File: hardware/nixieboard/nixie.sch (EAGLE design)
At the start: 60 parts

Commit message: added connectors to nixieboard for stability
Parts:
- added SV3, SV4: (no value), con-lstb:MA03-2
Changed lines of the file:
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@@
 <?xml version="1.0" encoding="utf-8"?>
 <!DOCTYPE eagle SYSTEM "eagle.dtd">
-<eagle version="7.2.0">
+<eagle version="6.5.0">
 <drawing>
 <settings>
@@
 <part name="SJ5" library="jumper" deviceset="SJ" device=""/>
 <part name="SJ6" library="jumper" deviceset="SJ" device=""/>
+<part name="SV3" library="con-lstb" deviceset="MA03-2" device=""/>
+<part name="SV4" library="con-lstb" deviceset="MA03-2" device=""/>
 </parts>
 <sheets>
@@
 <instance part="SJ5" gate="1" x="-180.34" y="7.62"/>
 <instance part="SJ6" gate="1" x="-180.34" y="2.54"/>
+<instance part="SV3" gate="1" x="-180.34" y="121.92"/>
+<instance part="SV4" gate="1" x="-180.34" y="106.68"/>
 </instances>
 <busses>

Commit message: added clock dots
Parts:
- added R25, R26, R27, R28: (no value), resistor:R-EU_R0805
- added SG1, SG2: F/CM12P, buzzer:F/CM12P
- added T21, T22: (no value), transistor:MMBTA42LT1-NPN-SOT23-BEC
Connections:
- new net DOT1: SG1.2, T21.C
- new net DOT2: SG2.2, T22.C
- new net DOTS: R27.1, R28.1, U$2.(OC1B)PB4
- new net N$28: R25.1, SG1.1
- new net N$29: R26.1, SG2.1
- new net N$30: R27.2, T21.B
- new net N$31: R28.2, T22.B
- net GND: now also T21.E, T22.E
- net HV: now also R25.2, R26.2
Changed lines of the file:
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@@
 <?xml version="1.0" encoding="utf-8"?>
 <!DOCTYPE eagle SYSTEM "eagle.dtd">
-<eagle version="6.5.0">
+<eagle version="6.6.0">
 <drawing>
 <settings>
@@
 <part name="SV3" library="con-lstb" deviceset="MA03-2" device=""/>
 <part name="SV4" library="con-lstb" deviceset="MA03-2" device=""/>
+<part name="SG1" library="buzzer" deviceset="F/CM12P" device=""/>
+<part name="SG2" library="buzzer" deviceset="F/CM12P" device=""/>
+<part name="R25" library="resistor" deviceset="R-EU_" device="R0805"/>
+<part name="R26" library="resistor" deviceset="R-EU_" device="R0805"/>
+<part name="T21" library="transistor" deviceset="*-NPN-" device="SOT23-BEC" technology="MMBTA42LT1"/>
+<part name="R27" library="resistor" deviceset="R-EU_" device="R0805"/>
+<part name="GND25" library="supply1" deviceset="GND" device=""/>
+<part name="T22" library="transistor" deviceset="*-NPN-" device="SOT23-BEC" technology="MMBTA42LT1"/>
+<part name="R28" library="resistor" deviceset="R-EU_" device="R0805"/>
+<part name="GND26" library="supply1" deviceset="GND" device=""/>
 </parts>
 <sheets>
@@
 <instance part="SV3" gate="1" x="-180.34" y="121.92"/>
 <instance part="SV4" gate="1" x="-180.34" y="106.68"/>
+<instance part="SG1" gate="G$1" x="60.96" y="35.56" rot="MR0"/>
+<instance part="SG2" gate="G$1" x="60.96" y="15.24" rot="MR0"/>
+<instance part="R25" gate="G$1" x="73.66" y="33.02"/>
+<instance part="R26" gate="G$1" x="73.66" y="12.7"/>
+<instance part="T21" gate="G$1" x="-27.94" y="-114.3"/>
+<instance part="R27" gate="G$1" x="-38.1" y="-114.3"/>
+<instance part="GND25" gate="1" x="-25.4" y="-121.92"/>
+<instance part="T22" gate="G$1" x="5.08" y="-114.3"/>
+<instance part="R28" gate="G$1" x="-5.08" y="-114.3"/>
+<instance part="GND26" gate="1" x="7.62" y="-121.92"/>
 </instances>
 <busses>
@@
 <label x="-195.58" y="-15.24" size="1.778" layer="95"/>
 </segment>
+<segment>
+<pinref part="T21" gate="G$1" pin="E"/>
+<pinref part="GND25" gate="1" pin="GND"/>
+</segment>
+<segment>
+<pinref part="T22" gate="G$1" pin="E"/>
+<pinref part="GND26" gate="1" pin="GND"/>
+</segment>
 </net>
 <net name="VCC_MC" class="0">
@@
 <label x="91.44" y="-45.72" size="1.778" layer="95" rot="MR0"/>
 </segment>
+<segment>
+<pinref part="R25" gate="G$1" pin="2"/>
+<wire x1="78.74" y1="33.02" x2="86.36" y2="33.02" width="0.1524" layer="91"/>
+<label x="86.36" y="33.02" size="1.778" layer="95" rot="MR0"/>
+</segment>
+<segment>
+<pinref part="R26" gate="G$1" pin="2"/>
+<wire x1="78.74" y1="12.7" x2="86.36" y2="12.7" width="0.1524" layer="91"/>
+<label x="86.36" y="12.7" size="1.778" layer="95" rot="MR0"/>
+</segment>
 </net>
 <net name="WS_OUT" class="0">
@@
 </segment>
 </net>
+<net name="DOTS" class="0">
+<segment>
+<pinref part="U$2" gate="G$1" pin="(OC1B)PB4"/>
+<wire x1="-81.28" y1="-27.94" x2="-68.58" y2="-27.94" width="0.1524" layer="91"/>
+<label x="-68.58" y="-27.94" size="1.778" layer="95" rot="MR0"/>
+</segment>
+<segment>
+<pinref part="R27" gate="G$1" pin="1"/>
+<wire x1="-43.18" y1="-114.3" x2="-50.8" y2="-114.3" width="0.1524" layer="91"/>
+<label x="-50.8" y="-114.3" size="1.778" layer="95"/>
+</segment>
+<segment>
+<pinref part="R28" gate="G$1" pin="1"/>
+<wire x1="-10.16" y1="-114.3" x2="-17.78" y2="-114.3" width="0.1524" layer="91"/>
+<label x="-17.78" y="-114.3" size="1.778" layer="95"/>
+</segment>
+</net>
+<net name="N$28" class="0">
+<segment>
+<pinref part="SG1" gate="G$1" pin="1"/>
+<pinref part="R25" gate="G$1" pin="1"/>
+<wire x1="68.58" y1="33.02" x2="63.5" y2="33.02" width="0.1524" layer="91"/>
+</segment>
+</net>
+<net name="N$29" class="0">
+<segment>
+<pinref part="SG2" gate="G$1" pin="1"/>
+<pinref part="R26" gate="G$1" pin="1"/>
+<wire x1="68.58" y1="12.7" x2="63.5" y2="12.7" width="0.1524" layer="91"/>
+</segment>
+</net>
+<net name="N$30" class="0">
+<segment>
+<pinref part="T21" gate="G$1" pin="B"/>
+<pinref part="R27" gate="G$1" pin="2"/>
+<wire x1="-33.02" y1="-114.3" x2="-30.48" y2="-114.3" width="0.1524" layer="91"/>
+</segment>
+</net>
+<net name="N$31" class="0">
+<segment>
+<pinref part="T22" gate="G$1" pin="B"/>
+<pinref part="R28" gate="G$1" pin="2"/>
+<wire x1="0" y1="-114.3" x2="2.54" y2="-114.3" width="0.1524" layer="91"/>
+</segment>
+</net>
+<net name="DOT1" class="0">
+<segment>
+<pinref part="SG1" gate="G$1" pin="2"/>
+<wire x1="55.88" y1="33.02" x2="45.72" y2="33.02" width="0.1524" layer="91"/>
+<label x="45.72" y="33.02" size="1.778" layer="95"/>
+</segment>
+<segment>
+<pinref part="T21" gate="G$1" pin="C"/>
+<wire x1="-25.4" y1="-109.22" x2="-25.4" y2="-106.68" width="0.1524" layer="91"/>
+<wire x1="-25.4" y1="-106.68" x2="-20.32" y2="-106.68" width="0.1524" layer="91"/>
+<label x="-20.32" y="-106.68" size="1.778" layer="95" rot="MR0"/>
+</segment>
+</net>
+<net name="DOT2" class="0">
+<segment>
+<pinref part="SG2" gate="G$1" pin="2"/>
+<wire x1="55.88" y1="12.7" x2="45.72" y2="12.7" width="0.1524" layer="91"/>
+<label x="45.72" y="12.7" size="1.778" layer="95"/>
+</segment>
+<segment>
+<pinref part="T22" gate="G$1" pin="C"/>
+<wire x1="7.62" y1="-109.22" x2="7.62" y2="-106.68" width="0.1524" layer="91"/>
+<wire x1="7.62" y1="-106.68" x2="12.7" y2="-106.68" width="0.1524" layer="91"/>
+<label x="12.7" y="-106.68" size="1.778" layer="95" rot="MR0"/>
+</segment>
+</net>

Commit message: fixed dot distances
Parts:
- SG1, SG2: device buzzer:F/CM12P -> ins1:F/CM12P
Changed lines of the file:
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@@
 <part name="SV3" library="con-lstb" deviceset="MA03-2" device=""/>
 <part name="SV4" library="con-lstb" deviceset="MA03-2" device=""/>
-<part name="SG1" library="buzzer" deviceset="F/CM12P" device=""/>
-<part name="SG2" library="buzzer" deviceset="F/CM12P" device=""/>
+<part name="SG1" library="ins1" deviceset="F/CM12P" device=""/>
+<part name="SG2" library="ins1" deviceset="F/CM12P" device=""/>
 <part name="R25" library="resistor" deviceset="R-EU_" device="R0805"/>
 <part name="R26" library="resistor" deviceset="R-EU_" device="R0805"/>

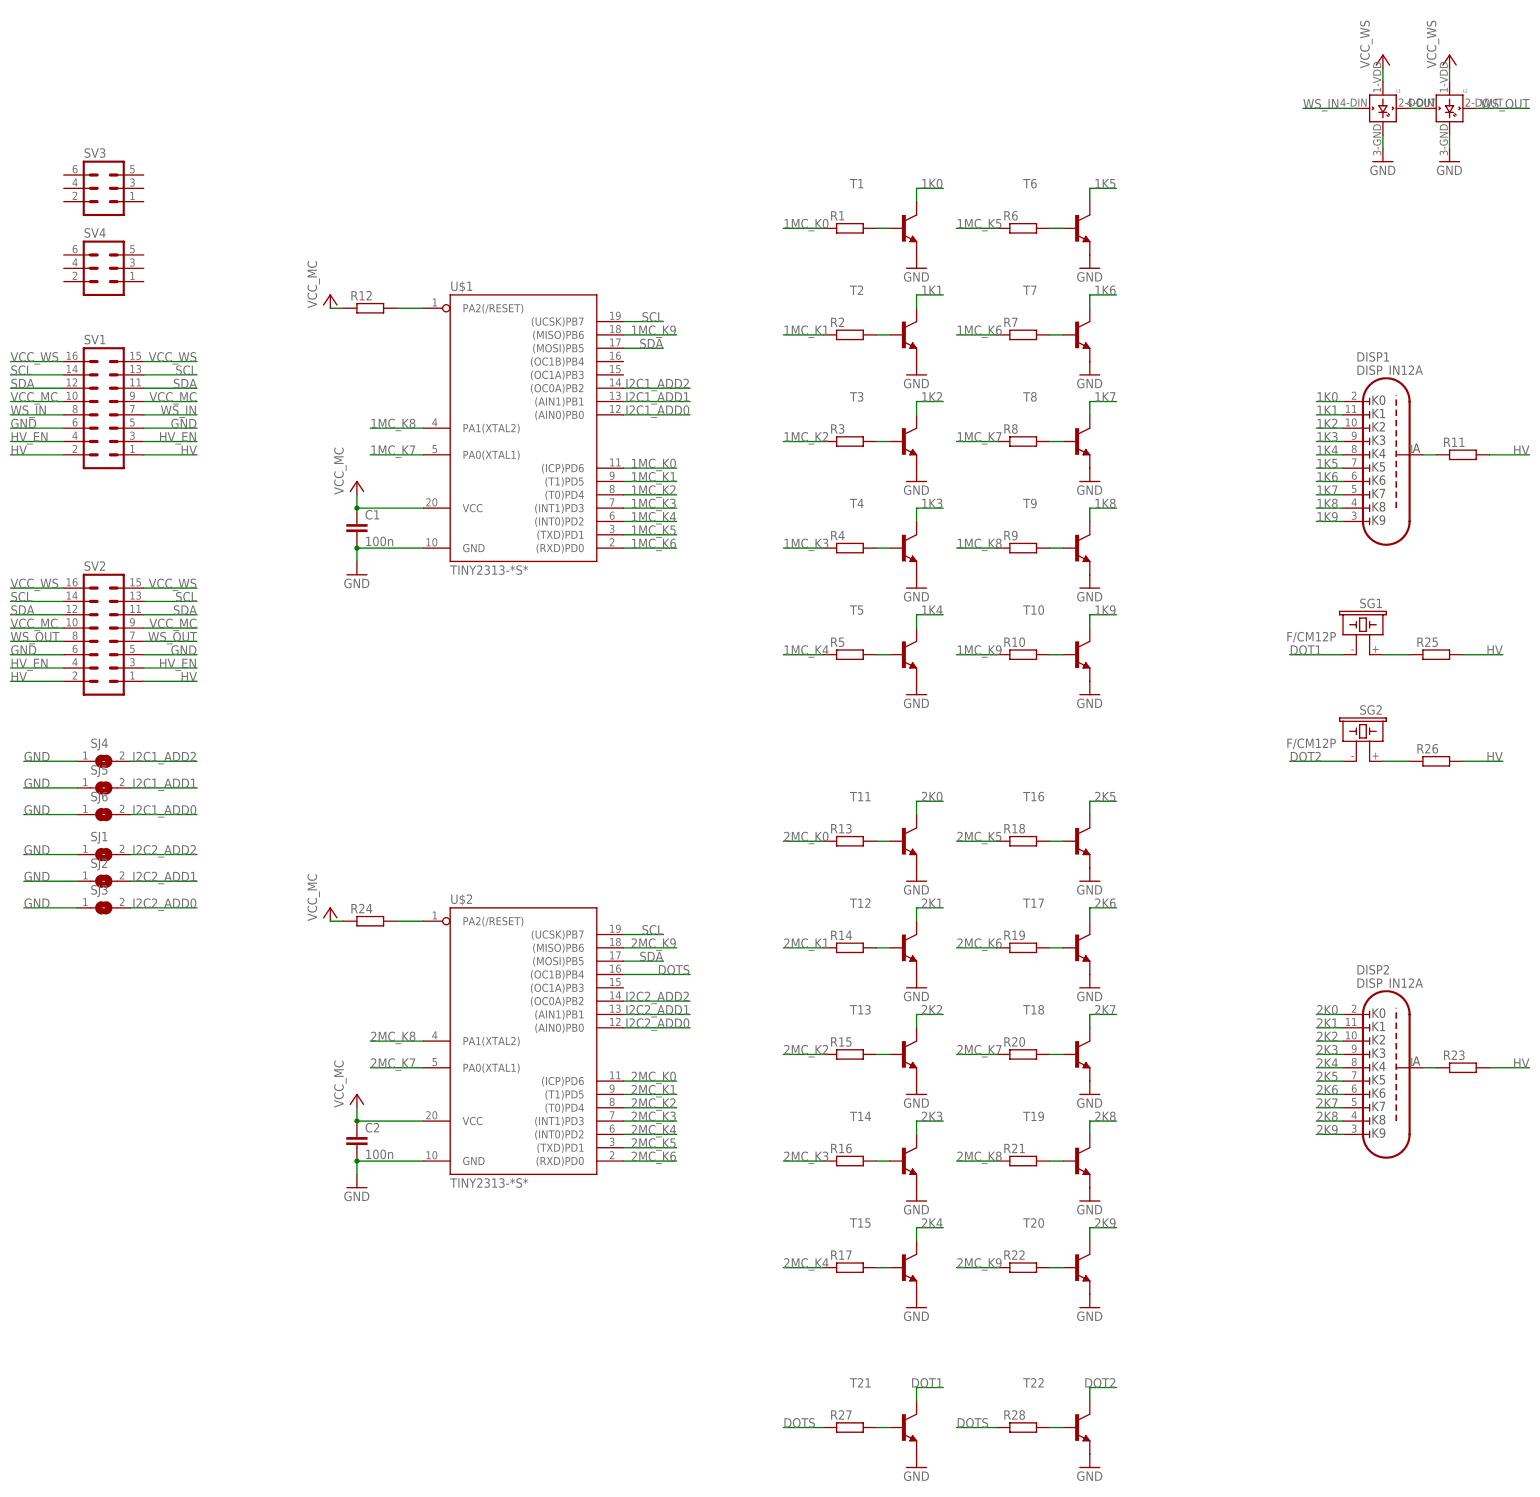
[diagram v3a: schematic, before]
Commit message: fix DP IN-12A Pinout
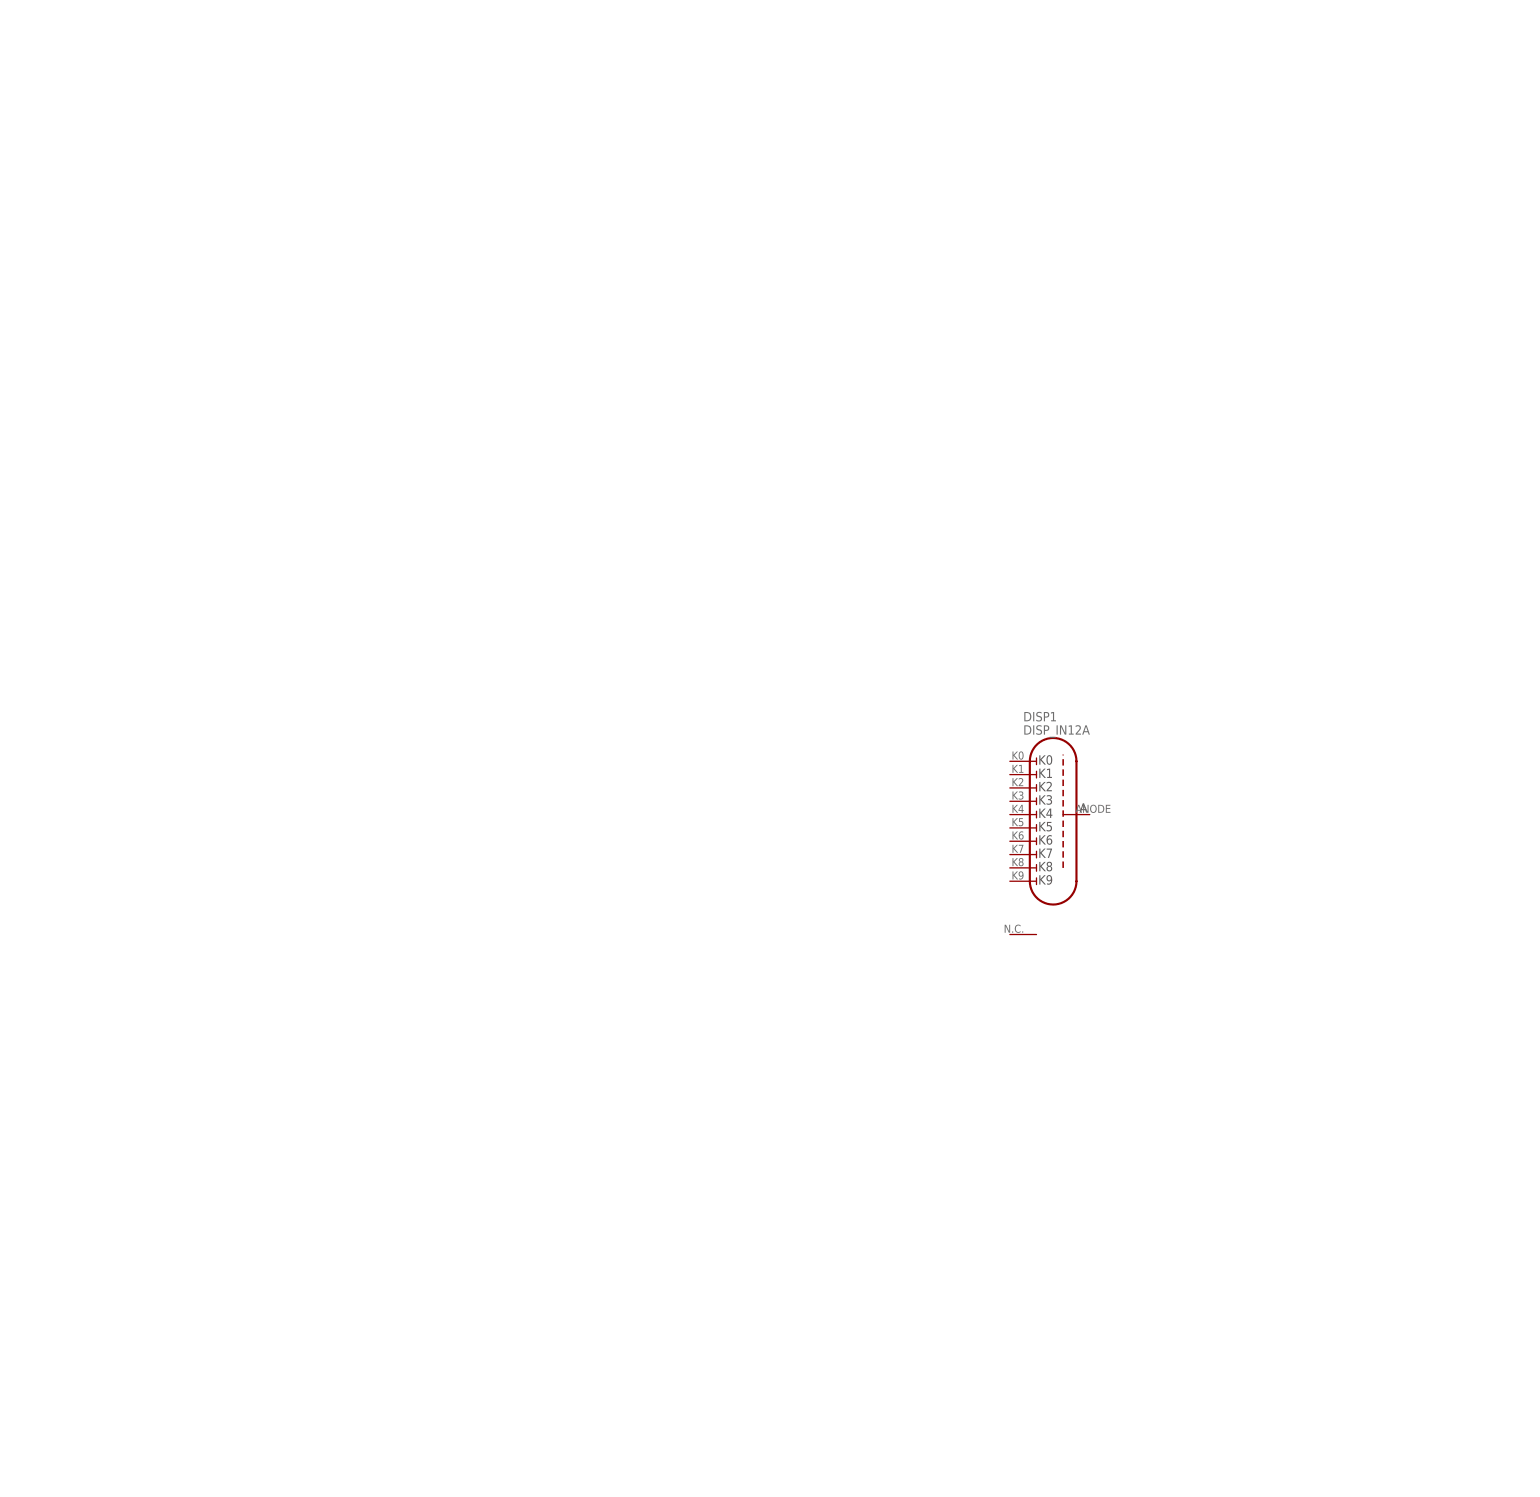
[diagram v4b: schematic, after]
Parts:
- removed C1, C2: 100n, rcl:C-EUC0805
- removed DISP2: DISP_IN12A, dp_devices:DISP_IN12A
- removed L1, L2: WS2812B, adafruit:WS2812B
- removed R1, R10, R11, R12, R13, R14, R15, R16, R17, R18, R19, R2, R20, R21, R22, R23, R24, R25, R26, R27, R28, R3, R4, R5, R6, R7, R8, R9: (no value), resistor:R-EU_R0805
- removed SG1, SG2: F/CM12P, ins1:F/CM12P
- removed SJ1, SJ2, SJ3, SJ4, SJ5, SJ6: (no value), jumper:SJ
- removed SV1, SV2: (no value), con-lstb:MA08-2
- removed SV3, SV4: (no value), con-lstb:MA03-2
- removed T1, T10, T11, T12, T13, T14, T15, T16, T17, T18, T19, T2, T20, T21, T22, T3, T4, T5, T6, T7, T8, T9: (no value), transistor:MMBTA42LT1-NPN-SOT23-BEC
- removed U$1, U$2: TINY2313-*S*, avr-6:TINY2313-*S*
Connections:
- removed net 1K0: DISP1.K0, T1.C
- removed net 1K1: DISP1.K1, T2.C
- removed net 1K2: DISP1.K2, T3.C
- removed net 1K3: DISP1.K3, T4.C
- removed net 1K4: DISP1.K4, T5.C
- removed net 1K5: DISP1.K5, T6.C
- removed net 1K6: DISP1.K6, T7.C
- removed net 1K7: DISP1.K7, T8.C
- removed net 1K8: DISP1.K8, T9.C
- removed net 1K9: DISP1.K9, T10.C
- removed net 1MC_K0: R1.1, U$1.(ICP)PD6
- removed net 1MC_K1: R2.1, U$1.(T1)PD5
- removed net 1MC_K2: R3.1, U$1.(T0)PD4
- removed net 1MC_K3: R4.1, U$1.(INT1)PD3
- removed net 1MC_K4: R5.1, U$1.(INT0)PD2
- removed net 1MC_K5: R6.1, U$1.(TXD)PD1
- removed net 1MC_K6: R7.1, U$1.(RXD)PD0
- removed net 1MC_K7: R8.1, U$1.PA0(XTAL1)
- removed net 1MC_K8: R9.1, U$1.PA1(XTAL2)
- removed net 1MC_K9: R10.1, U$1.(MISO)PB6
- removed net 2K0: DISP2.K0, T11.C
- removed net 2K1: DISP2.K1, T12.C
- removed net 2K2: DISP2.K2, T13.C
- removed net 2K3: DISP2.K3, T14.C
- removed net 2K4: DISP2.K4, T15.C
- removed net 2K5: DISP2.K5, T16.C
- removed net 2K6: DISP2.K6, T17.C
- removed net 2K7: DISP2.K7, T18.C
- removed net 2K8: DISP2.K8, T19.C
- removed net 2K9: DISP2.K9, T20.C
- removed net 2MC_K0: R13.1, U$2.(ICP)PD6
- removed net 2MC_K1: R14.1, U$2.(T1)PD5
- removed net 2MC_K2: R15.1, U$2.(T0)PD4
- removed net 2MC_K3: R16.1, U$2.(INT1)PD3
- removed net 2MC_K4: R17.1, U$2.(INT0)PD2
- removed net 2MC_K5: R18.1, U$2.(TXD)PD1
- removed net 2MC_K6: R19.1, U$2.(RXD)PD0
- removed net 2MC_K7: R20.1, U$2.PA0(XTAL1)
- removed net 2MC_K8: R21.1, U$2.PA1(XTAL2)
- removed net 2MC_K9: R22.1, U$2.(MISO)PB6
- removed net DOT1: SG1.2, T21.C
- removed net DOT2: SG2.2, T22.C
- removed net DOTS: R27.1, R28.1, U$2.(OC1B)PB4
- removed net GND: C1.2, C2.2, L1.GND, L2.GND, SJ1.1, SJ2.1, SJ3.1, SJ4.1, SJ5.1, SJ6.1, SV1.5, SV1.6, SV2.5, SV2.6, T1.E, T10.E, T11.E, T12.E, T13.E, T14.E, T15.E, T16.E, T17.E, T18.E, T19.E, T2.E, T20.E, T21.E, T22.E, T3.E, T4.E, T5.E, T6.E, T7.E, T8.E, T9.E, U$1.GND, U$2.GND
- removed net HV: R11.2, R23.2, R25.2, R26.2, SV1.1, SV1.2, SV2.1, SV2.2
- removed net HV_EN: SV1.3, SV1.4, SV2.3, SV2.4
- removed net I2C1_ADD0: SJ6.2, U$1.(AIN0)PB0
- removed net I2C1_ADD1: SJ5.2, U$1.(AIN1)PB1
- removed net I2C1_ADD2: SJ4.2, U$1.(OC0A)PB2
- removed net I2C2_ADD0: SJ3.2, U$2.(AIN0)PB0
- removed net I2C2_ADD1: SJ2.2, U$2.(AIN1)PB1
- removed net I2C2_ADD2: SJ1.2, U$2.(OC0A)PB2
- removed net N$1: R2.2, T2.B
- removed net N$10: R1.2, T1.B
- removed net N$11: DISP1.ANODE, R11.1
- removed net N$12: R13.2, T11.B
- removed net N$13: R12.2, U$1.PA2(/RESET)
- removed net N$14: R14.2, T12.B
- removed net N$15: R15.2, T13.B
- removed net N$16: R16.2, T14.B
- removed net N$17: R17.2, T15.B
- removed net N$18: R18.2, T16.B
- removed net N$19: R19.2, T17.B
- removed net N$2: R3.2, T3.B
- removed net N$20: R20.2, T18.B
- removed net N$21: R21.2, T19.B
- removed net N$22: R22.2, T20.B
- removed net N$23: R24.2, U$2.PA2(/RESET)
- removed net N$24: DISP2.ANODE, R23.1
- removed net N$25: L1.DOUT, L2.DIN
- removed net N$28: R25.1, SG1.1
- removed net N$29: R26.1, SG2.1
- removed net N$3: R4.2, T4.B
- removed net N$30: R27.2, T21.B
- removed net N$31: R28.2, T22.B
- removed net N$4: R5.2, T5.B
- removed net N$5: R6.2, T6.B
- removed net N$6: R7.2, T7.B
- removed net N$7: R8.2, T8.B
- removed net N$8: R9.2, T9.B
- removed net N$9: R10.2, T10.B
- removed net SCL: SV1.13, SV1.14, SV2.13, SV2.14, U$1.(UCSK)PB7, U$2.(UCSK)PB7
- removed net SDA: SV1.11, SV1.12, SV2.11, SV2.12, U$1.(MOSI)PB5, U$2.(MOSI)PB5
- removed net VCC_MC: C1.1, C2.1, R12.1, R24.1, SV1.10, SV1.9, SV2.10, SV2.9, U$1.VCC, U$2.VCC
- removed net VCC_WS: L1.VDD, L2.VDD, SV1.15, SV1.16, SV2.15, SV2.16
- removed net WS_IN: L1.DIN, SV1.7, SV1.8
- removed net WS_OUT: L2.DOUT, SV2.7, SV2.8
